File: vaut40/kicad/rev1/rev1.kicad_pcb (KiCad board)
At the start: 2 copper layers, 228.3 x 128.1 mm, 82 parts, among them SW1 SW_PUSH, SW10 SW_PUSH, SW11 SW_PUSH, SW12 SW_PUSH, SW13 SW_PUSH, SW14 SW_PUSH, SW15 SW_PUSH, SW16 SW_PUSH, SW17 SW_PUSH, SW18 SW_PUSH, SW19 SW_PUSH, SW2 SW_PUSH, SW20 SW_PUSH, SW21 SW_PUSH, SW22 SW_PUSH, SW23 SW_PUSH, SW24 SW_PUSH, SW25 SW_PUSH, SW26 SW_PUSH, SW27 SW_PUSH, SW28 SW_PUSH, SW29 SW_PUSH, SW3 SW_PUSH, SW30 SW_PUSH, SW31 SW_PUSH, SW32 SW_PUSH, SW33 SW_PUSH, SW34 SW_PUSH, SW35 SW_PUSH, SW36 SW_PUSH, SW37 SW_PUSH, SW38 SW_PUSH, SW39 SW_PUSH, SW4 SW_PUSH, SW40 SW_PUSH, SW41 SW_PUSH, SW5 SW_PUSH, SW6 SW_PUSH, SW7 SW_PUSH, SW8 SW_PUSH, SW9 SW_PUSH, U1 ProMicro_r

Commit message: routing
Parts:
- moved SW41 4.26 mm to (179.4, 40.4)
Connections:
- D10 pad 1: Row2 -> Row0
- D11 pad 1: Row0 -> Row1
- D12 pad 1: Row0 -> Row1
- D13 pad 1: Row0 -> Row1
- D14 pad 1: Row0 -> Row1
- D15 pad 1: Row0 -> Row1
- D16 pad 1: Row2 -> Row1
- D17 pad 1: Row2 -> Row1
- D18 pad 1: Row2 -> Row1
- D19 pad 1: Row2 -> Row1
- D20 pad 1: Row2 -> Row1
- D21 pad 1: Row1 -> Row2
- D22 pad 1: Row1 -> Row2
- D23 pad 1: Row1 -> Row2
- D24 pad 1: Row1 -> Row2
- D25 pad 1: Row1 -> Row2
- D26 pad 1: Row3 -> Row2
- D27 pad 1: Row3 -> Row2
- D28 pad 1: Row3 -> Row2
- D29 pad 1: Row3 -> Row2
- D30 pad 1: Row3 -> Row2
- D31 pad 1: Row1 -> Row3
- D32 pad 1: Row1 -> Row3
- D33 pad 1: Row1 -> Row3
- D34 pad 1: Row1 -> Row3
- D35 pad 1: Row1 -> Row3
- D6 pad 1: Row2 -> Row0
- D7 pad 1: Row2 -> Row0
- D8 pad 1: Row2 -> Row0
- D9 pad 1: Row2 -> Row0
- SW1 pad 1: Column3 -> Column0
- SW10 pad 1: Column4 -> Column9
- SW11 pad 1: Column8 -> Column0
- SW12 pad 1: Column6 -> Column1
- SW13 pad 1: Column5 -> Column2
- SW14 pad 1: Column7 -> Column3
- SW15 pad 1: Column9 -> Column4
- SW16 pad 1: Column8 -> Column5
- SW18 pad 1: Column5 -> Column7
- SW19 pad 1: Column7 -> Column8
- SW21 pad 1: Column3 -> Column0
- SW23 pad 1: Column0 -> Column2
- SW24 pad 1: Column2 -> Column3
- SW26 pad 1: Column3 -> Column5
- SW27 pad 1: Column1 -> Column6
- SW28 pad 1: Column0 -> Column7
- SW29 pad 1: Column2 -> Column8
- SW3 pad 1: Column0 -> Column2
- SW30 pad 1: Column4 -> Column9
- SW31 pad 1: Column6 -> Column0
- SW32 pad 1: Column5 -> Column1
- SW33 pad 1: Column7 -> Column2
- SW34 pad 1: Column8 -> Column3
- SW35 pad 1: Column9 -> Column4
- SW36 pad 1: Column9 -> Column5
- SW37 pad 1: Column8 -> Column6
- SW38 pad 1: Column6 -> Column7
- SW39 pad 1: Column5 -> Column8
- SW4 pad 1: Column2 -> Column3
- SW40 pad 1: Column7 -> Column9
- SW6 pad 1: Column3 -> Column5
- SW7 pad 1: Column1 -> Column6
- SW8 pad 1: Column0 -> Column7
- SW9 pad 1: Column2 -> Column8
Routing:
- net Row3: track 0.00 -> 329.2 mm, vias 0 -> 2
- net Row2: track 0.00 -> 288.9 mm, vias 0 -> 2
- net Row1: track 0.00 -> 262.8 mm, vias 0 -> 2
- net Row0: track 0.00 -> 237.4 mm
- net Column0: track 0.00 -> 168.5 mm
- net Column1: track 0.00 -> 150.2 mm
- net Column2: track 0.00 -> 148.8 mm
- net Column9: track 0.00 -> 145.3 mm, vias 0 -> 2
- net Column3: track 0.00 -> 129.8 mm
- net Column8: track 0.00 -> 122.1 mm, vias 0 -> 2
- net Column4: track 0.00 -> 117.4 mm
- net Column7: track 0.00 -> 109.9 mm
- net Column5: track 0.00 -> 107.8 mm
- net Column6: track 0.00 -> 104.4 mm
- net Net-(D39-A): track 0.00 -> 14.8 mm
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
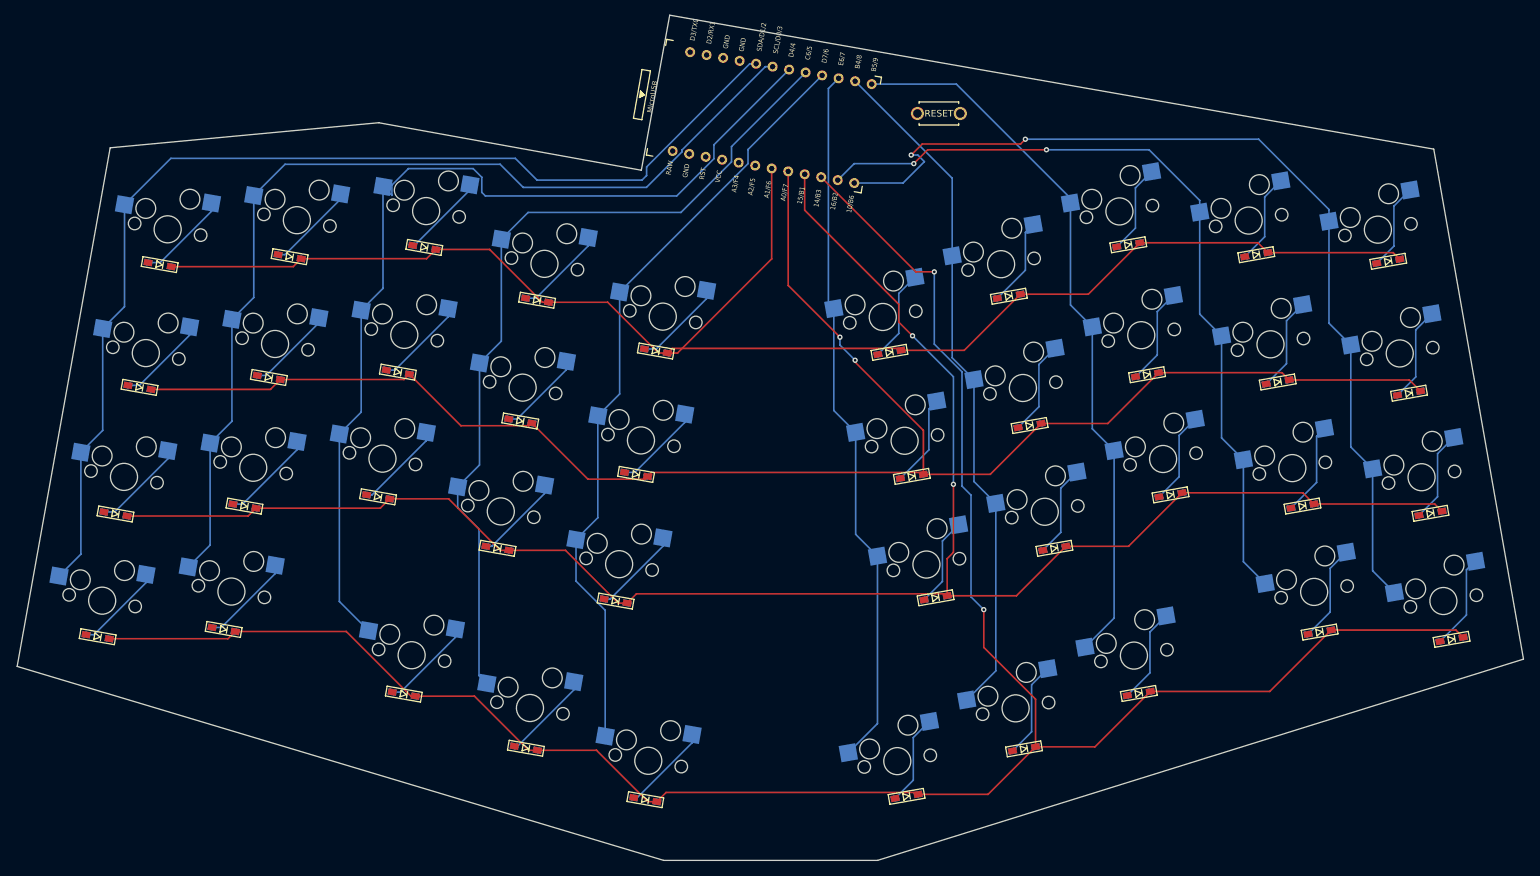
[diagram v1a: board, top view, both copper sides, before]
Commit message: add hole
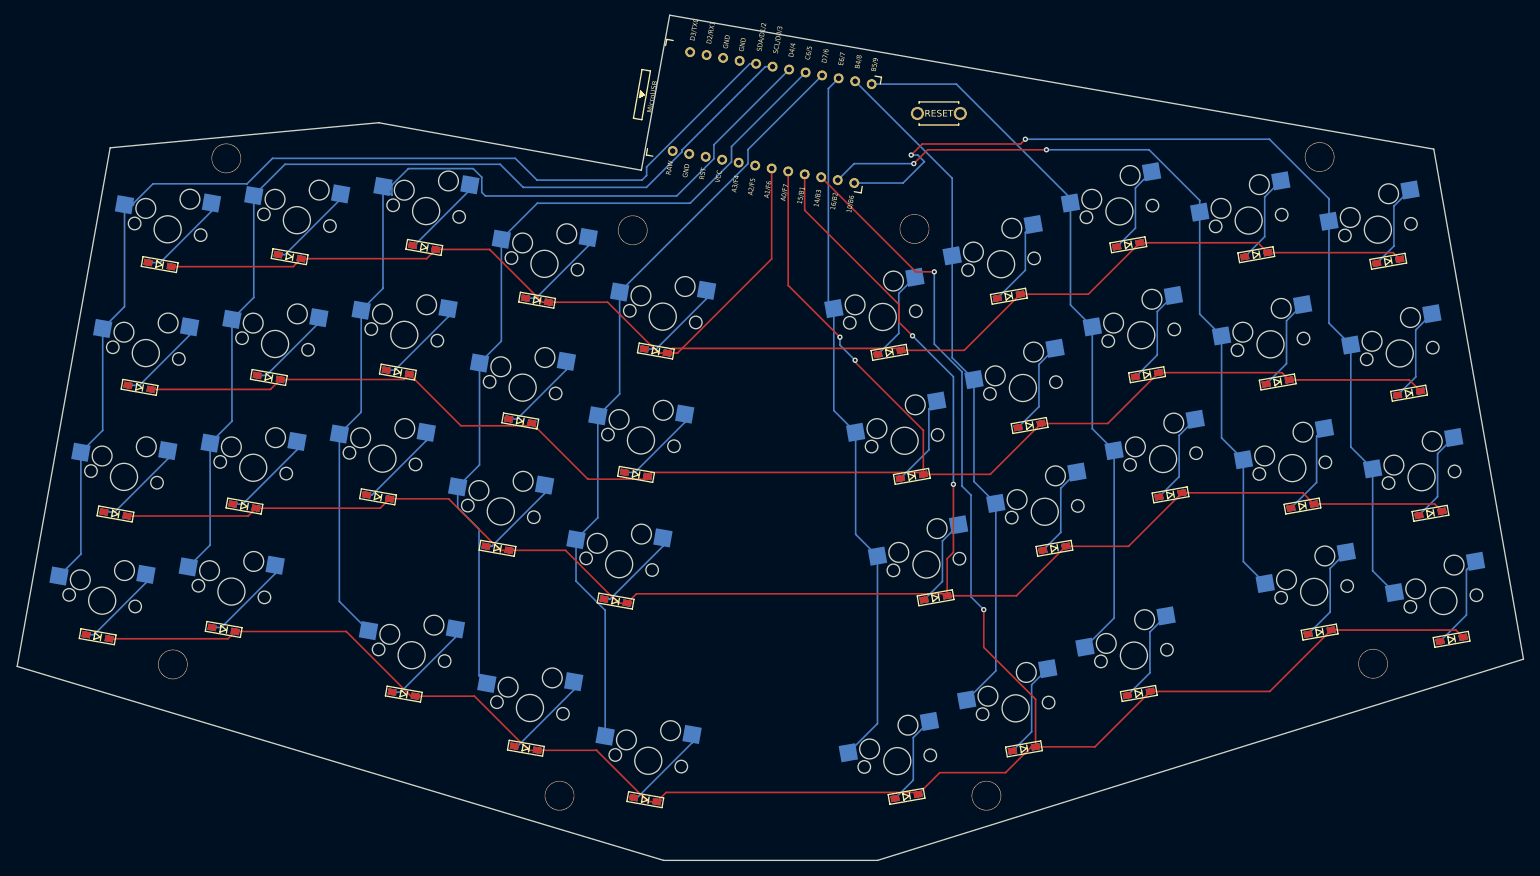
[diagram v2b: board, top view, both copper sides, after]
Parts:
- added Ref**: Val**, kbd_Hole:m2_Spacer_Hole, F.Cu at (245.2, 123.8)
- added Ref**: Val**, kbd_Hole:m2_Spacer_Hole, F.Cu at (71.4, 47.2)
- added Ref**: Val**, kbd_Hole:m2_Spacer_Hole, F.Cu at (63.3, 123.9)
- added Ref**: Val**, kbd_Hole:m2_Spacer_Hole, F.Cu at (121.9, 143.8)
- added Ref**: Val**, kbd_Hole:m2_Spacer_Hole, F.Cu at (175.7, 57.9)
- added Ref**: Val**, kbd_Hole:m2_Spacer_Hole, F.Cu at (186.6, 143.8)
- added Ref**: Val**, kbd_Hole:m2_Spacer_Hole, F.Cu at (133.0, 58.1)
- added Ref**: Val**, kbd_Hole:m2_Spacer_Hole, F.Cu at (237.1, 47.0)
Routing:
- net Column9: track 145.3 -> 146.2 mm

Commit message: add GND
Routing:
- net GND: track 0.00 -> 36.8 mm
- net Net-(U1-RST): track 0.00 -> 34.8 mm
- added copper zone on B.Cu, net GND
- added copper zone on F.Cu, net GND
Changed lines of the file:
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@@
   (segment (start 238.517071 72.189286) (end 241.825071 75.497286) (width 0.25) (layer "B.Cu") (net 54))
   (segment (start 245.133071 109.710486) (end 248.441071 113.018486) (width 0.25) (layer "B.Cu") (net 54))
+  (segment (start 181.325 39.075) (end 155.850239 39.075) (width 0.25) (layer "F.Cu") (net 55))
+  (segment (start 182.65 40.4) (end 181.325 39.075) (width 0.25) (layer "F.Cu") (net 55))
+  (segment (start 155.850239 39.075) (end 149.196794 32.421555) (width 0.25) (layer "F.Cu") (net 55))
+  (segment (start 176.15 40.4) (end 150.62172 40.4) (width 0.25) (layer "F.Cu") (net 56))
+  (segment (start 150.62172 40.4) (end 144.052457 46.969263) (width 0.25) (layer "F.Cu") (net 56))
+  (zone (net 55) (net_name "GND") (layer "F.Cu") (hatch edge 0.5)
+    (connect_pads (clearance 0.5))
+    (min_thickness 0.25) (filled_areas_thickness no)
+    (fill yes (thermal_gap 0.5) (thermal_bridge_width 0.5))
+    (polygon
+      (pts
+        (xy 138.6 25.2)
+        (xy 134.2 48.7)
+        (xy 94.3 41.3)
+        (xy 53.1 45)
+        (xy 39.1 124.3)
+        (xy 137.4 154)
+        (xy 170.2 154)
+        (xy 268.5 123.2)
+        (xy 254.9 45.5)
+        (xy 138.6 25.3)
+      )
+    )
+  )
+  (zone (net 55) (net_name "GND") (layer "B.Cu") (hatch edge 0.5)
+    (priority 1)
+    (connect_pads (clearance 0.5))
+    (min_thickness 0.25) (filled_areas_thickness no)
+    (fill yes (thermal_gap 0.5) (thermal_bridge_width 0.5))
+    (polygon
+      (pts
+        (xy 138.6 25.2)
+        (xy 134.2 48.7)
+        (xy 94.3 41.3)
+        (xy 53.1 45)
+        (xy 39.1 124.3)
+        (xy 137.4 154)
+        (xy 170.2 154)
+        (xy 268.5 123.2)
+        (xy 254.9 45.5)
+      )
+    )
+  )
 )

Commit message: fix error of pcb
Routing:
- net Row1: track 262.8 -> 290.5 mm, vias 2 -> 12
- net Row0: track 237.4 -> 261.3 mm, vias 0 -> 10
- net Row3: track 329.2 -> 350.5 mm, vias 2 -> 12
- net Row2: track 288.9 -> 308.9 mm, vias 2 -> 12
- net Net-(D37-A): track 14.7 -> 20.0 mm, vias 0 -> 1
- net Net-(D40-A): track 14.4 -> 18.4 mm, vias 0 -> 1
- net Net-(D31-A): track 13.6 -> 17.4 mm, vias 0 -> 1
- net Net-(D29-A): track 14.2 -> 17.7 mm, vias 0 -> 1
- net Net-(D39-A): track 14.8 -> 18.2 mm, vias 0 -> 1
- net Net-(D23-A): track 13.7 -> 16.9 mm, vias 0 -> 1
- net Net-(D22-A): track 14.4 -> 17.4 mm, vias 0 -> 1
- net Net-(D12-A): track 13.4 -> 16.2 mm, vias 0 -> 1
- net Net-(D18-A): track 14.7 -> 17.4 mm, vias 0 -> 1
- net Net-(D35-A): track 13.5 -> 16.3 mm, vias 0 -> 1
- net Net-(D1-A): track 14.1 -> 16.8 mm, vias 0 -> 1
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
